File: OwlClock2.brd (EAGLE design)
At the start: 160 x 100 mm, 96 parts, among them IC1 MCP1703DB, J1 AVR_SPI_PRG_6NS, J2 POWER_JACKPTH, U1 ATMEGA328P_PDIP

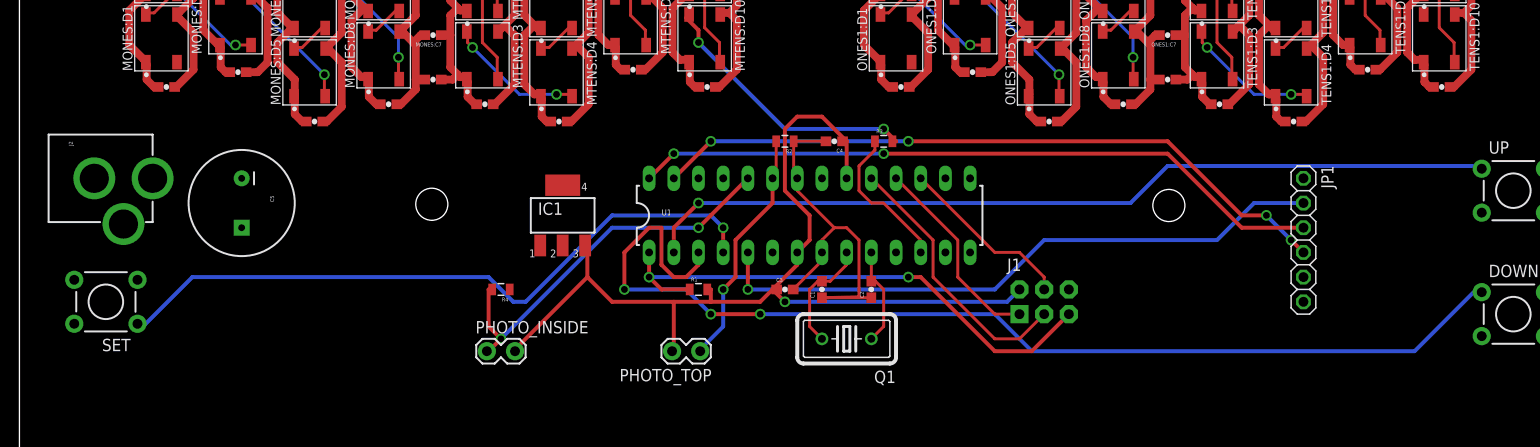
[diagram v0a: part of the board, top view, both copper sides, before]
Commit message: Add vias for led grounds, clean up switches, fix up the supply caps.
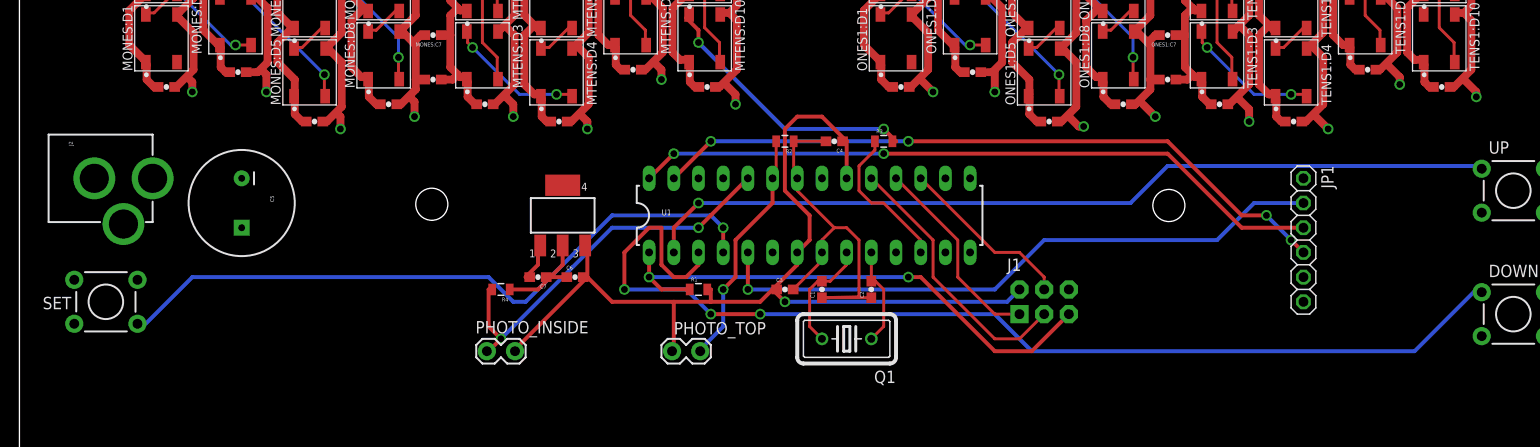
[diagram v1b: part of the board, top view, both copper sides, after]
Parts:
- added C6, C7: 1uF, SparkFun-Capacitors:0603-CAP
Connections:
- net GND: now also C6.1, C7.1
- net VCC: now also C5.1, C7.2
- net VSS: now also C6.2; no longer C5.1
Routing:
- net GND: track 430.7 -> 441.3 mm
- net VCC: track 336.1 -> 340.4 mm
- net N$19: track 0.00 -> 2.71 mm, vias 0 -> 1
- net N$21: track 0.00 -> 2.56 mm, vias 0 -> 1
- net N$5: track 0.00 -> 2.50 mm, vias 0 -> 1
- net N$12: track 0.00 -> 2.45 mm, vias 0 -> 1
- net N$9: track 0.00 -> 2.35 mm, vias 0 -> 1
- net N$22: track 0.00 -> 2.30 mm, vias 0 -> 1
- net N$8: track 0.00 -> 2.24 mm, vias 0 -> 1
- net N$11: track 0.00 -> 2.09 mm, vias 0 -> 1
- net N$14: track 0.00 -> 2.03 mm, vias 0 -> 1
- net N$15: track 0.00 -> 1.94 mm, vias 0 -> 1
- net N$10: track 0.00 -> 1.84 mm, vias 0 -> 1
- net N$20: track 0.00 -> 1.80 mm, vias 0 -> 1
- net N$16: track 0.00 -> 1.80 mm, vias 0 -> 1
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
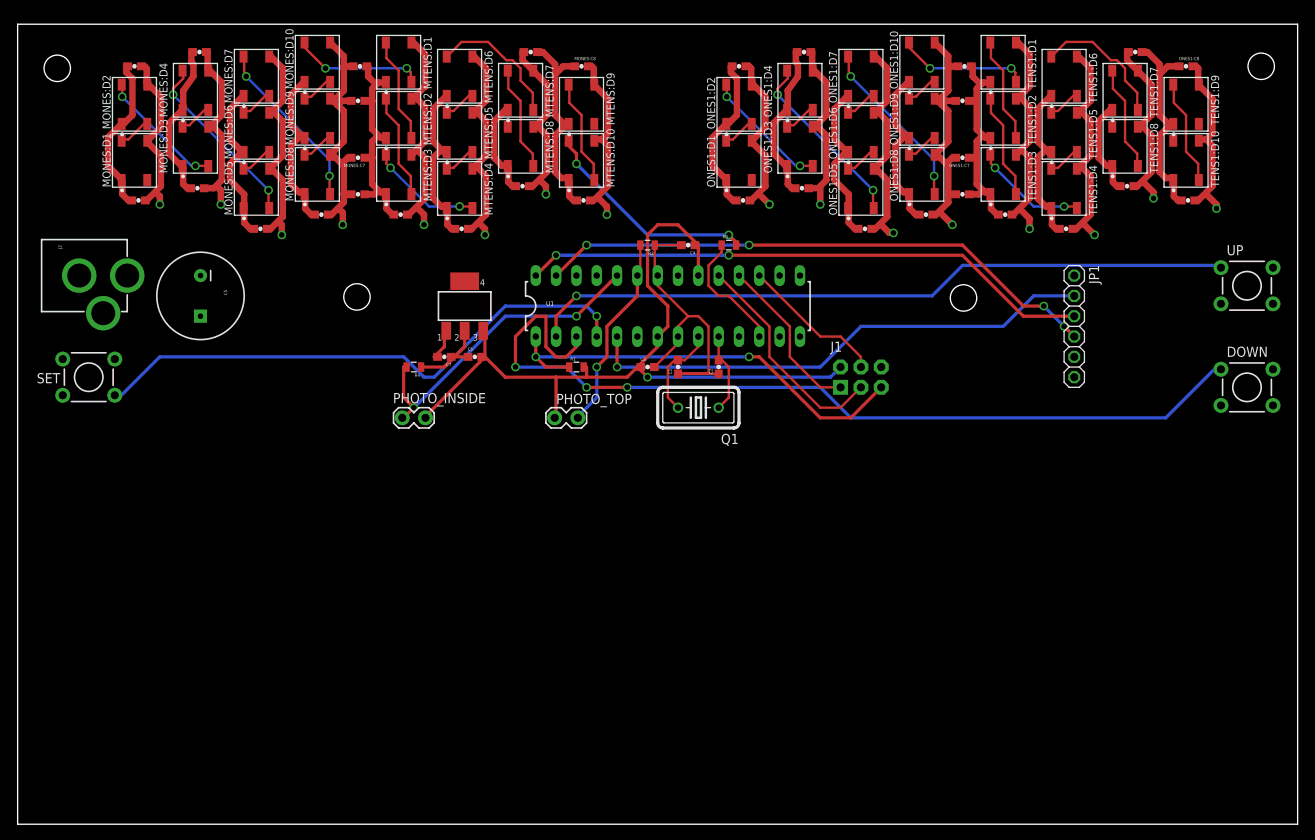
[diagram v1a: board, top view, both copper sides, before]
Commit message: More work on ground plane, fixed ground vias for led power.
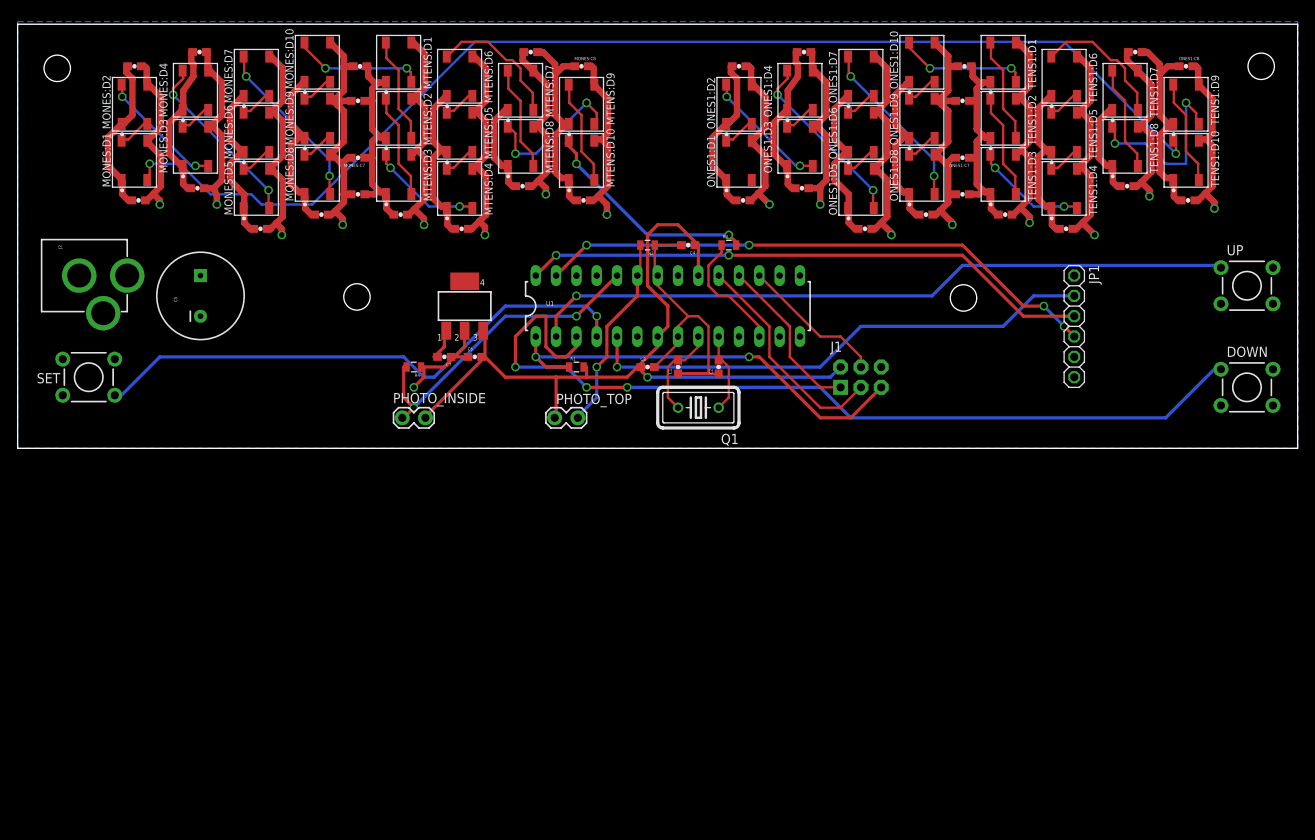
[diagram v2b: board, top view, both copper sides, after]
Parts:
- turned C5 to 90 degrees
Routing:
- net M_ONES_OUT: track 0.00 -> 148.4 mm, vias 0 -> 2
- net GND: track 441.3 -> 479.2 mm, vias 0 -> 17
- net TENS1:N$13: track 0.00 -> 24.1 mm, vias 0 -> 2
- net MTENS:N$13: track 0.00 -> 19.8 mm, vias 0 -> 2
- net N$19: track 2.71 -> 0.00 mm, vias 1 -> 0
- net N$21: track 2.56 -> 0.00 mm, vias 1 -> 0
- net N$5: track 2.50 -> 0.00 mm, vias 1 -> 0
- net N$12: track 2.45 -> 0.00 mm, vias 1 -> 0
- net N$9: track 2.35 -> 0.00 mm, vias 1 -> 0
- net N$22: track 2.30 -> 0.00 mm, vias 1 -> 0
- net N$8: track 2.24 -> 0.00 mm, vias 1 -> 0
- net N$11: track 2.09 -> 0.00 mm, vias 1 -> 0
- net N$14: track 2.03 -> 0.00 mm, vias 1 -> 0
- net N$15: track 1.94 -> 0.00 mm, vias 1 -> 0
- net N$10: track 1.84 -> 0.00 mm, vias 1 -> 0
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- added copper zone on layer 16, net GND
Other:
- board size 160 x 100 mm -> 160 x 53 mm

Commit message: Add power plane fix board outline, finish first pass of routing.
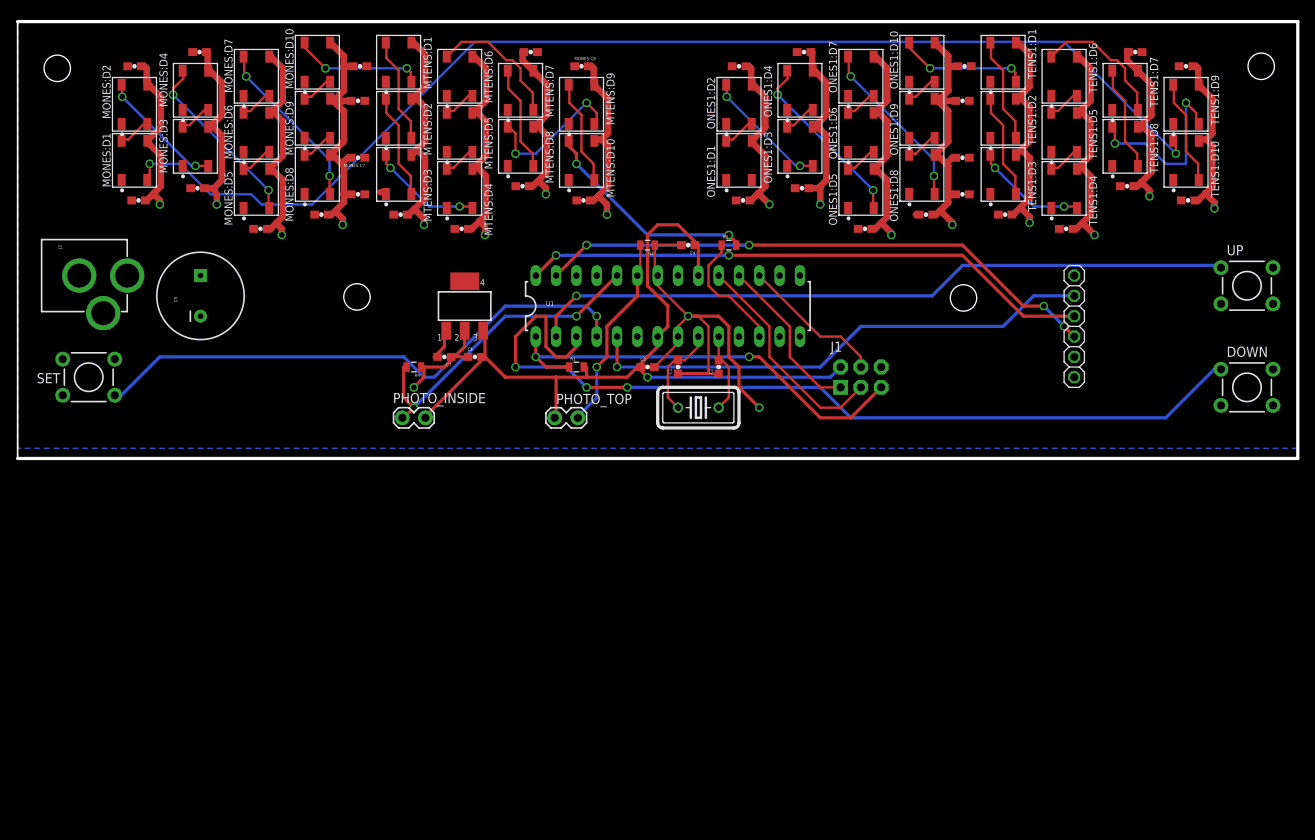
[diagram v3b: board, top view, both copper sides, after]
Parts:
- C5: value (none) -> 1000uF
- JP1: value (none) -> REAL TIME CLOCK
- Q1: value (none) -> 16Mhz
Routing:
- net VCC: track 340.4 -> 6.74 mm
- net GND: track 479.2 -> 497.9 mm, vias 17 -> 19
- added copper zone on layer 1, net VCC
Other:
- board size 160 x 53 mm -> 160 x 54.6 mm

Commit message: Finish up labels and cleanup, pass design rules check
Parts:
- C2: value 0.22pF -> 22pF
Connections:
- net 32K: now also U1.15
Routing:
- net 32K: track 0.00 -> 37.4 mm, vias 0 -> 1
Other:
- board text added: "32K"
- board text added: "GND"
- board text added: "Owl Clock"
- board text added: "V1.0"
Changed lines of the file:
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@@
 <wire x1="160.02" y1="45.72" x2="160.02" y2="100.33" width="0.4064" layer="20"/>
 <wire x1="160.02" y1="100.33" x2="0" y2="100.33" width="0.4064" layer="20"/>
+<text x="134.112" y="55.245" size="1.016" layer="21">GND</text>
+<text x="134.239" y="68.199" size="1.016" layer="21">32K</text>
+<text x="110.49" y="52.07" size="1.4224" layer="21">Owl Clock</text>
+<text x="110.49" y="49.53" size="1.4224" layer="21">V1.0</text>
 </plain>
 <attributes>
@@
 </autorouter>
 <elements>
-<element name="C1" library="SparkFun-Capacitors" package="0603-CAP" value="22pF" x="82.55" y="57.15" rot="R90">
+<element name="C1" library="SparkFun-Capacitors" package="0603-CAP" value="22pF" x="82.55" y="57.15" smashed="yes" rot="R90">
 <attribute name="PROD_ID" value="CAP-00810" x="82.55" y="57.15" size="1.778" layer="27" rot="R90" display="off"/>
-</element>
-<element name="C2" library="SparkFun-Capacitors" package="0603-CAP" value="0.22pF" x="87.63" y="57.15" rot="R90">
+<attribute name="VALUE" x="83.693" y="56.134" size="0.4064" layer="27" font="vector" rot="R90"/>
+</element>
+<element name="C2" library="SparkFun-Capacitors" package="0603-CAP" value="22pF" x="87.63" y="57.15" smashed="yes" rot="R90">
 <attribute name="PROD_ID" value="CAP-00810" x="87.63" y="57.15" size="1.778" layer="27" rot="R90" display="off"/>
-</element>
-<element name="C3" library="SparkFun-Capacitors" package="0603-CAP" value="0.1uF" x="78.74" y="57.15">
+<attribute name="VALUE" x="88.773" y="56.134" size="0.4064" layer="27" font="vector" rot="R90"/>
+</element>
+<element name="C3" library="SparkFun-Capacitors" package="0603-CAP" value="0.1uF" x="78.74" y="57.15" smashed="yes">
 <attribute name="PROD_ID" value="CAP-00810" x="78.74" y="57.15" size="1.778" layer="27" display="off"/>
-</element>
-<element name="C4" library="SparkFun-Capacitors" package="0603-CAP" value="0.1uF" x="83.82" y="72.39" rot="R180">
+<attribute name="VALUE" x="78.232" y="57.912" size="0.4064" layer="27" font="vector"/>
+</element>
+<element name="C4" library="SparkFun-Capacitors" package="0603-CAP" value="0.1uF" x="83.82" y="72.39" smashed="yes" rot="R180">
 <attribute name="PROD_ID" value="CAP-00810" x="83.82" y="72.39" size="1.778" layer="27" rot="R180" display="off"/>
-</element>
-<element name="J1" library="SparkFun-Connectors" package="2X3-NS" value="AVR_SPI_PRG_6NS" x="105.41" y="55.88" smashed="yes">
-<attribute name="NAME" x="101.6" y="59.055" size="1.27" layer="25" ratio="10"/>
-</element>
+<attribute name="VALUE" x="84.836" y="73.533" size="0.4064" layer="27" font="vector" rot="R180"/>
+</element>
+<element name="J1" library="SparkFun-Connectors" package="2X3-NS" value="AVR_SPI_PRG_6NS" x="105.41" y="55.88" smashed="yes"/>
 <element name="J2" library="SparkFun-Connectors" package="POWER_JACK_PTH" value="POWER_JACKPTH" x="0" y="68.58" rot="R270">
 <attribute name="PROD_ID" value="PRT-00119" x="0" y="68.58" size="1.778" layer="27" rot="R270" display="off"/>
@@
 <attribute name="VALUE" x="96.52" y="50.3428" size="1.27" layer="27" ratio="10" rot="R180"/>
 </element>
-<element name="R1" library="SparkFun-Resistors" package="0805" value="10k" x="69.85" y="57.15">
+<element name="R1" library="SparkFun-Resistors" package="0805" value="10k" x="69.85" y="57.15" smashed="yes">
 <attribute name="PROD_ID" value="RES-09883" x="69.85" y="57.15" size="1.778" layer="27" display="off"/>
-</element>
-<element name="R2" library="SparkFun-Resistors" package="0805" value="10k" x="78.74" y="72.39" rot="R180">
+<attribute name="VALUE" x="69.596" y="55.753" size="0.4064" layer="27"/>
+</element>
+<element name="R2" library="SparkFun-Resistors" package="0805" value="10k" x="78.74" y="72.39" smashed="yes" rot="R180">
 <attribute name="PROD_ID" value="RES-09883" x="78.74" y="72.39" size="1.778" layer="27" rot="R180" display="off"/>
+<attribute name="VALUE" x="79.756" y="73.787" size="0.4064" layer="27" rot="R180"/>
 </element>
 <element name="UP" library="SparkFun-Electromechanical" package="TACTILE-PTH" value="SWITCH-MOMENTARY-2PTH" x="153.67" y="67.31"/>
@@
 <attribute name="NAME" x="5.334" y="56.388" size="1.27" layer="25" ratio="10" rot="R180"/>
 </element>
-<element name="R3" library="SparkFun-Resistors" package="0805" value="470" x="88.9" y="72.39">
+<element name="R3" library="SparkFun-Resistors" package="0805" value="470" x="88.9" y="72.39" smashed="yes">
 <attribute name="PROD_ID" value="RES-09883" x="88.9" y="72.39" size="1.778" layer="27" display="off"/>
+<attribute name="VALUE" x="87.122" y="73.152" size="0.4064" layer="27"/>
 </element>
 <element name="C5" library="SparkFun-Capacitors" package="CPOL-RADIAL-1000UF-25V" value="1000uF" x="22.86" y="66.04" rot="R90"/>
@@
 <attribute name="NAME" x="46.9138" y="52.6288" size="1.27" layer="25" ratio="10"/>
 </element>
-<element name="R4" library="SparkFun-Resistors" package="0805" value="10k" x="49.53" y="57.15" rot="R180">
+<element name="R4" library="SparkFun-Resistors" package="0805" value="10k" x="49.53" y="57.15" smashed="yes" rot="R180">
 <attribute name="PROD_ID" value="RES-09883" x="53.34" y="53.34" size="1.778" layer="27" rot="R180" display="off"/>
+<attribute name="VALUE" x="50.038" y="58.674" size="0.4064" layer="27" rot="R180"/>
 </element>
 <element name="IC1" library="linear" package="SOT223" value="MCP1703DB" x="55.88" y="64.77" smashed="yes">
 <attribute name="VALUE" x="52.07" y="60.9092" size="1.27" layer="27" rot="R90"/>
 </element>
-<element name="C6" library="SparkFun-Capacitors" package="0603-CAP" value="1uF" x="57.15" y="58.42">
+<element name="C6" library="SparkFun-Capacitors" package="0603-CAP" value="1uF" x="57.15" y="58.42" smashed="yes">
 <attribute name="PROD_ID" value="CAP-00810" x="57.15" y="58.42" size="1.778" layer="27" display="off"/>
-</element>
-<element name="C7" library="SparkFun-Capacitors" package="0603-CAP" value="1uF" x="53.34" y="58.42" rot="R180">
+<attribute name="VALUE" x="56.769" y="57.15" size="0.4064" layer="27" font="vector"/>
+</element>
+<element name="C7" library="SparkFun-Capacitors" package="0603-CAP" value="1uF" x="53.34" y="58.42" smashed="yes" rot="R180">
 <attribute name="PROD_ID" value="CAP-00810" x="53.34" y="58.42" size="1.778" layer="27" rot="R180" display="off"/>
+<attribute name="VALUE" x="54.102" y="57.531" size="0.4064" layer="27" font="vector" rot="R180"/>
 </element>
 </elements>
@@
 <signal name="32K">
 <contactref element="JP1" pad="1"/>
+<contactref element="U1" pad="15"/>
+<wire x1="129.54" y1="71.12" x2="132.08" y2="68.58" width="0.3048" layer="1"/>
+<wire x1="118.11" y1="71.12" x2="129.54" y2="71.12" width="0.3048" layer="16"/>
+<wire x1="114.3" y1="67.31" x2="118.11" y2="71.12" width="0.3048" layer="16"/>
+<wire x1="99.06" y1="67.31" x2="114.3" y2="67.31" width="0.3048" layer="16"/>
+<wire x1="97.79" y1="68.58" x2="99.06" y2="67.31" width="0.3048" layer="16"/>
+<via x="129.54" y="71.12" extent="1-16" drill="0.7"/>
 </signal>
 <signal name="SQW">
